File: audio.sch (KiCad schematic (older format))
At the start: 47 parts, among them Q11 BC546, Q12 BC546, Q13 BC546, Q14 BC546, U4 TL072

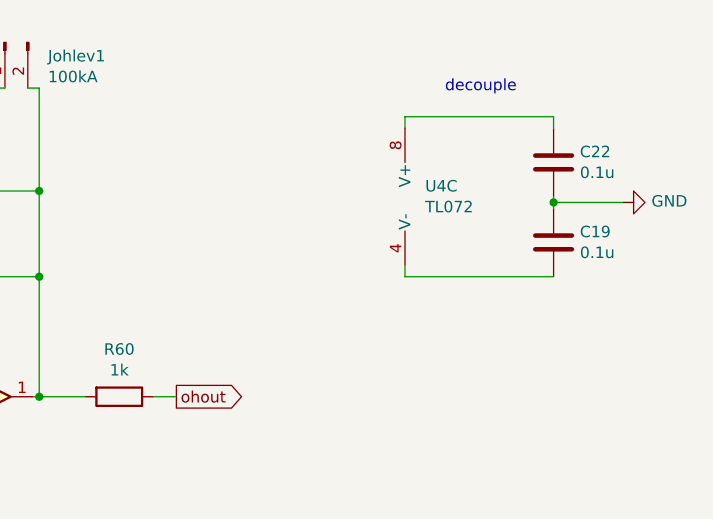
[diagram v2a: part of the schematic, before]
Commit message: fixup noise generator connections
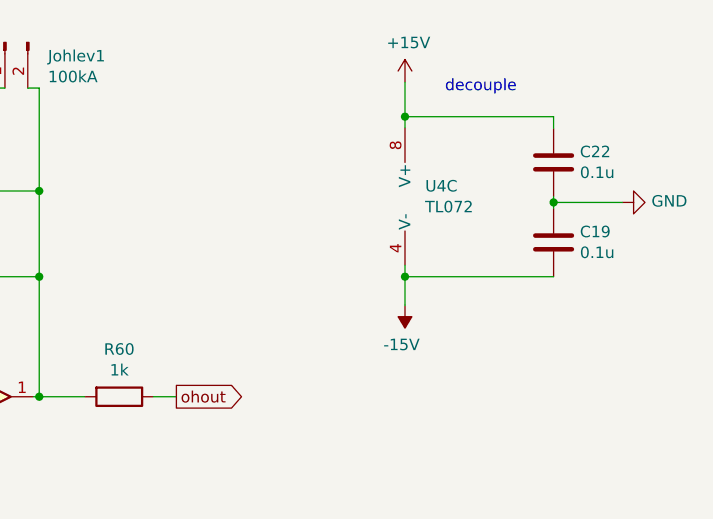
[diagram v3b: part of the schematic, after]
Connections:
- net +15V: now also C22.1, U4.8 (V+)
- net -15V: now also C19.2, U4.4 (V-)
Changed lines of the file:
@@
 EESchema Schematic File Version 4
 LIBS:808-hats-cache
-LIBS:shift-triggers-cache
-LIBS:mod-dac-cache
 EELAYER 26 0
 EELAYER END
@@
 Text Notes 9025 1000 0    50   ~ 0
 decouple
+$Comp
+L power:+15V #PWR?
+U 1 1 5CB7A0F9
+P 8850 950
+AR Path="/5CB7A0F9" Ref="#PWR?"  Part="1"
+AR Path="/5CC0DBBF/5CB7A0F9" Ref="#PWR0148"  Part="1"
+F 0 "#PWR0148" H 8850 800 50  0001 C CNN
+F 1 "+15V" H 8865 1123 50  0000 C CNN
+F 2 "" H 8850 950 50  0001 C CNN
+F 3 "" H 8850 950 50  0001 C CNN
+	1    8850 950
+	1    0    0    -1
+$EndComp
+$Comp
+L power:-15V #PWR?
+U 1 1 5CB7A166
+P 8850 1925
+AR Path="/5CB7A166" Ref="#PWR?"  Part="1"
+AR Path="/5CC0DBBF/5CB7A166" Ref="#PWR0149"  Part="1"
+F 0 "#PWR0149" H 8850 2025 50  0001 C CNN
+F 1 "-15V" H 8865 2098 50  0000 C CNN
+F 2 "" H 8850 1925 50  0001 C CNN
+F 3 "" H 8850 1925 50  0001 C CNN
+	1    8850 1925
+	-1   0    0    1
+$EndComp
+Wire Wire Line
+	8850 1800 8850 1925
+Connection ~ 8850 1800
+Wire Wire Line
+	8850 1100 8850 950
+Connection ~ 8850 1100
 $EndSCHEMATC

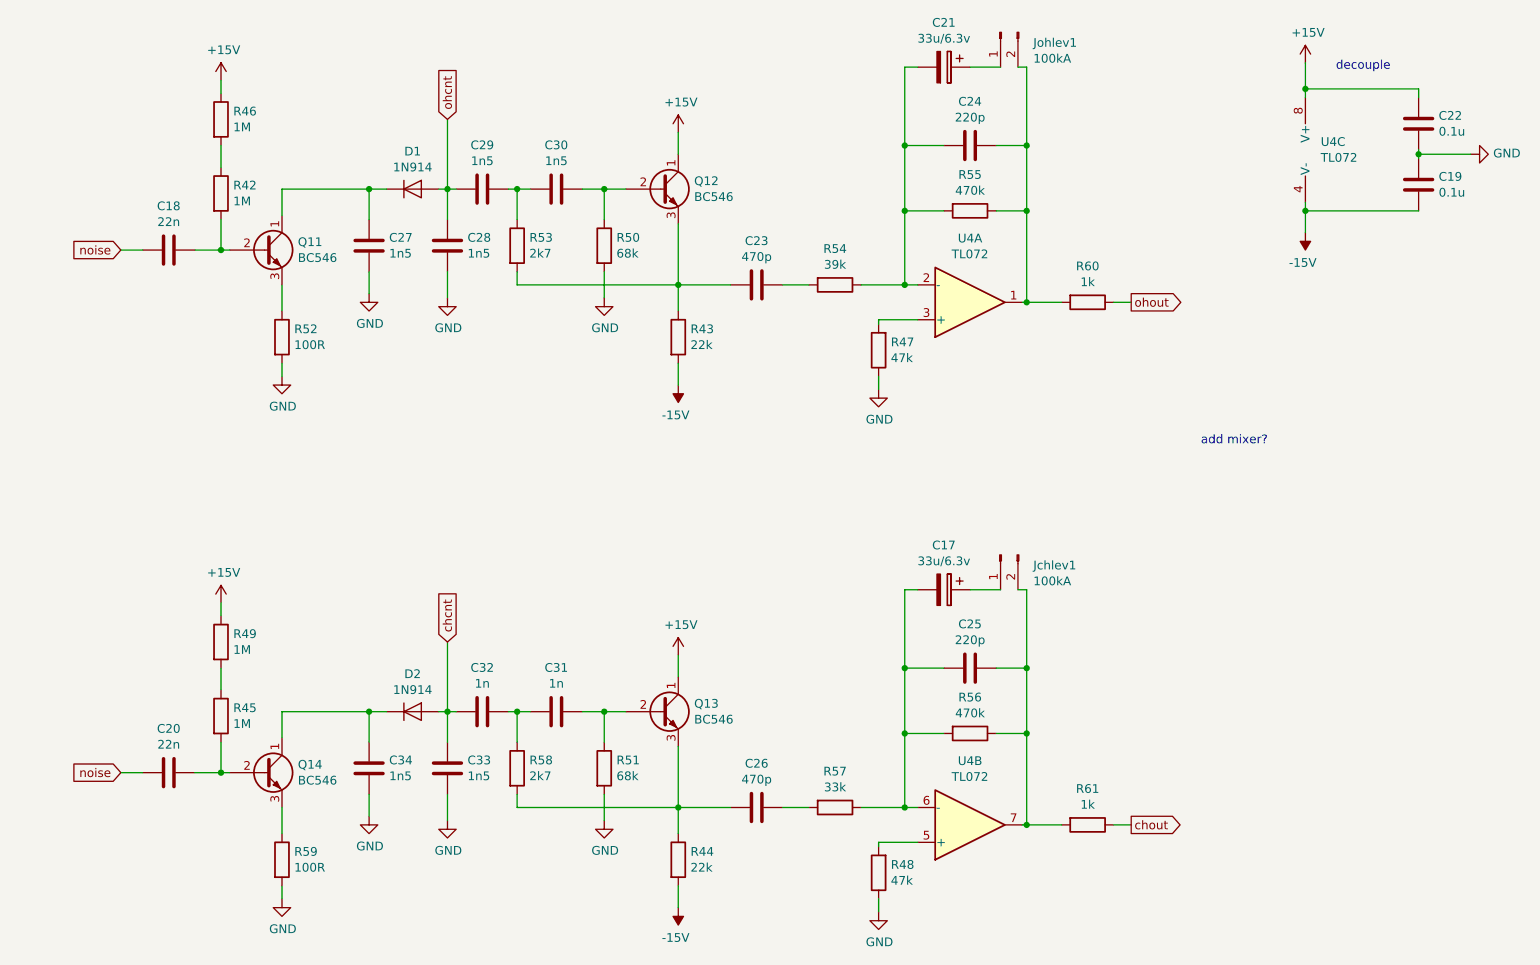
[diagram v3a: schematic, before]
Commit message: added filter mod
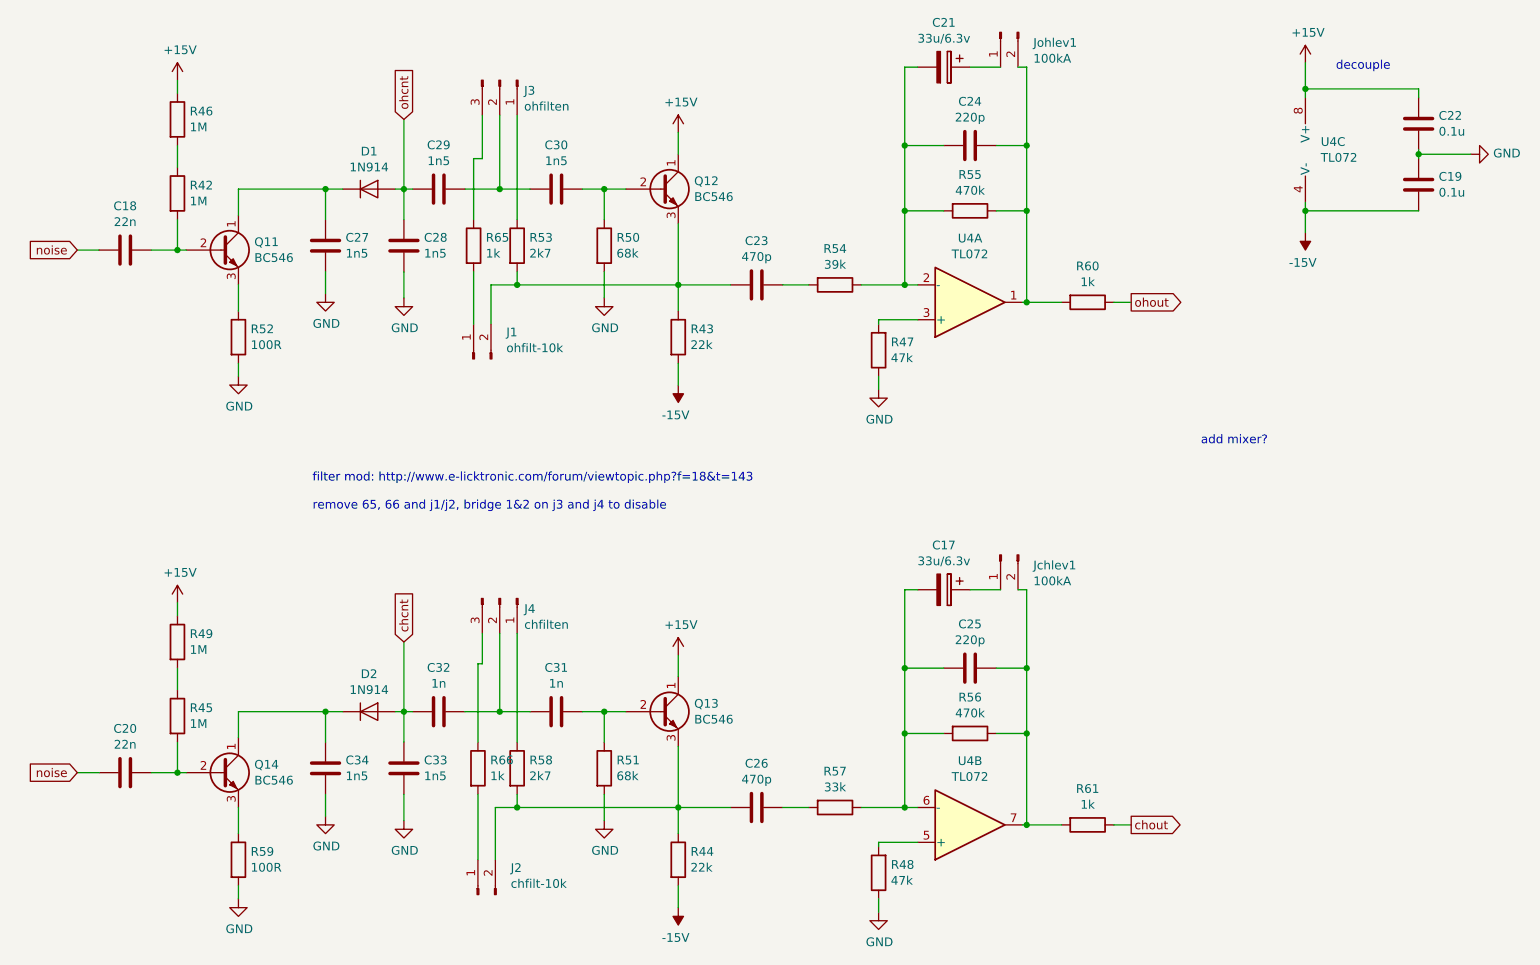
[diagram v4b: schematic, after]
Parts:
- added J1: ohfilt-10k, symbol Connector:Conn_01x02_Male
- added J2: chfilt-10k, symbol Connector:Conn_01x02_Male
- added J3: ohfilten, symbol Connector:Conn_01x03_Male
- added J4: chfilten, symbol Connector:Conn_01x03_Male
- added R65, R66: 1k, symbol Device:R
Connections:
- net at C29.2, C30.1: now also J3.2 (Pin_2); no longer R53.1
- net at C23.1, Q12.3 (E), R43.1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: now also J1.2 (Pin_2)
- net at C31.1, C32.2: now also J4.2 (Pin_2); no longer R58.1
- net at C26.1, Q13.3 (E), R44.1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: now also J2.2 (Pin_2)
- new net: J3.1 (Pin_1), R53.1
- new net: J3.3 (Pin_3), R65.1
- new net: J1.1 (Pin_1), R65.2
- new net: J4.1 (Pin_1), R58.1
- new net: J4.3 (Pin_3), R66.1
- new net: J2.1 (Pin_1), R66.2
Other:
- note added: "filter mod: http://www.e-licktronic.com/forum/viewtopic.php?f=18&t=143\n\nremove 65, 66 and j1/j2, bridge 1&2 on j3 and j4 to disable"
- moved on the sheet: C18, C20, C27, C28, C29, C32, C33, C34, D1, D2, Q11, Q14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

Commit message: selected some parts
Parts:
- C17: footprint (none) -> Capacitor_THT:CP_Radial_D7.5mm_P2.50mm
- J1, J2, Jchlev1, Johlev1: footprint (none) -> Connector_PinHeader_2.54mm:PinHeader_1x02_P2.54mm_Vertical
- J3, J4: footprint (none) -> Connector_PinHeader_2.54mm:PinHeader_1x03_P2.54mm_Vertical
- Q11, Q12, Q13, Q14: footprint Package_TO_SOT_THT:TO-92_Inline -> Package_TO_SOT_THT:TO-92L_Inline
- R42, R43, R44, R45, R46, R47, R48, R49, R50, R51, R52, R53, R54, R55, R56, R57, R58, R59, R60, R61, R65, R66: footprint (none) -> Resistor_THT:R_Axial_DIN0204_L3.6mm_D1.6mm_P7.62mm_Horizontal
- U4: footprint (none) -> Package_DIP:DIP-8_W7.62mm_LongPads
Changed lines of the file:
@@
 F 0 "R42" H 2445 1746 50  0000 L CNN
 F 1 "1M" H 2445 1655 50  0000 L CNN
-F 2 "" V 2305 1700 50  0001 C CNN
+F 2 "Resistor_THT:R_Axial_DIN0204_L3.6mm_D1.6mm_P7.62mm_Horizontal" V 2305 1700 50  0001 C CNN
 F 3 "~" H 2375 1700 50  0001 C CNN
 	1    2375 1700
@@
 F 0 "R46" H 2445 1321 50  0000 L CNN
 F 1 "1M" H 2445 1230 50  0000 L CNN
-F 2 "" V 2305 1275 50  0001 C CNN
+F 2 "Resistor_THT:R_Axial_DIN0204_L3.6mm_D1.6mm_P7.62mm_Horizontal" V 2305 1275 50  0001 C CNN
 F 3 "~" H 2375 1275 50  0001 C CNN
 	1    2375 1275
@@
 F 0 "Q11" H 2816 2071 50  0000 L CNN
 F 1 "BC546" H 2816 1980 50  0000 L CNN
-F 2 "Package_TO_SOT_THT:TO-92_Inline" H 2825 1950 50  0001 L CIN
+F 2 "Package_TO_SOT_THT:TO-92L_Inline" H 2825 1950 50  0001 L CIN
 F 3 "http://www.fairchildsemi.com/ds/BC/BC547.pdf" H 2625 2025 50  0001 L CNN
 	1    2625 2025
@@
 F 0 "R52" H 2795 2571 50  0000 L CNN
 F 1 "100R" H 2795 2480 50  0000 L CNN
-F 2 "" V 2655 2525 50  0001 C CNN
+F 2 "Resistor_THT:R_Axial_DIN0204_L3.6mm_D1.6mm_P7.62mm_Horizontal" V 2655 2525 50  0001 C CNN
 F 3 "~" H 2725 2525 50  0001 C CNN
 	1    2725 2525
@@
 F 0 "R53" H 4395 2046 50  0000 L CNN
 F 1 "2k7" H 4395 1955 50  0000 L CNN
-F 2 "" V 4255 2000 50  0001 C CNN
+F 2 "Resistor_THT:R_Axial_DIN0204_L3.6mm_D1.6mm_P7.62mm_Horizontal" V 4255 2000 50  0001 C CNN
 F 3 "~" H 4325 2000 50  0001 C CNN
 	1    4325 2000
@@
 F 0 "R50" H 4895 2046 50  0000 L CNN
 F 1 "68k" H 4895 1955 50  0000 L CNN
-F 2 "" V 4755 2000 50  0001 C CNN
+F 2 "Resistor_THT:R_Axial_DIN0204_L3.6mm_D1.6mm_P7.62mm_Horizontal" V 4755 2000 50  0001 C CNN
 F 3 "~" H 4825 2000 50  0001 C CNN
 	1    4825 2000
@@
 F 0 "Q12" H 5341 1721 50  0000 L CNN
 F 1 "BC546" H 5341 1630 50  0000 L CNN
-F 2 "Package_TO_SOT_THT:TO-92_Inline" H 5350 1600 50  0001 L CIN
+F 2 "Package_TO_SOT_THT:TO-92L_Inline" H 5350 1600 50  0001 L CIN
 F 3 "http://www.fairchildsemi.com/ds/BC/BC547.pdf" H 5150 1675 50  0001 L CNN
 	1    5150 1675
@@
 F 0 "R43" H 5320 2571 50  0000 L CNN
 F 1 "22k" H 5320 2480 50  0000 L CNN
-F 2 "" V 5180 2525 50  0001 C CNN
+F 2 "Resistor_THT:R_Axial_DIN0204_L3.6mm_D1.6mm_P7.62mm_Horizontal" V 5180 2525 50  0001 C CNN
 F 3 "~" H 5250 2525 50  0001 C CNN
 	1    5250 2525
@@
 F 0 "R54" V 5943 2225 50  0000 C CNN
 F 1 "39k" V 6034 2225 50  0000 C CNN
-F 2 "" V 6080 2225 50  0001 C CNN
+F 2 "Resistor_THT:R_Axial_DIN0204_L3.6mm_D1.6mm_P7.62mm_Horizontal" V 6080 2225 50  0001 C CNN
 F 3 "~" H 6150 2225 50  0001 C CNN
 	1    6150 2225
@@
 F 0 "U4" H 6925 1958 50  0000 C CNN
 F 1 "TL072" H 6925 2049 50  0000 C CNN
-F 2 "" H 6925 2325 50  0001 C CNN
+F 2 "Package_DIP:DIP-8_W7.62mm_LongPads" H 6925 2325 50  0001 C CNN
 F 3 "http://www.ti.com/lit/ds/symlink/tl071.pdf" H 6925 2325 50  0001 C CNN
 	1    6925 2325
@@
 F 0 "R47" H 6330 2554 50  0000 R CNN
 F 1 "47k" H 6330 2645 50  0000 R CNN
-F 2 "" V 6330 2600 50  0001 C CNN
+F 2 "Resistor_THT:R_Axial_DIN0204_L3.6mm_D1.6mm_P7.62mm_Horizontal" V 6330 2600 50  0001 C CNN
 F 3 "~" H 6400 2600 50  0001 C CNN
 	1    6400 2600
@@
 F 0 "R55" V 6718 1800 50  0000 C CNN
 F 1 "470k" V 6809 1800 50  0000 C CNN
-F 2 "" V 6855 1800 50  0001 C CNN
+F 2 "Resistor_THT:R_Axial_DIN0204_L3.6mm_D1.6mm_P7.62mm_Horizontal" V 6855 1800 50  0001 C CNN
 F 3 "~" H 6925 1800 50  0001 C CNN
 	1    6925 1800
@@
 F 0 "Johlev1" V 7160 587 50  0000 R CNN
 F 1 "100kA" V 7251 587 50  0000 R CNN
-F 2 "" H 7100 775 50  0001 C CNN
+F 2 "Connector_PinHeader_2.54mm:PinHeader_1x02_P2.54mm_Vertical" H 7100 775 50  0001 C CNN
 F 3 "~" H 7100 775 50  0001 C CNN
 	1    7100 775
@@
 F 0 "R60" V 7393 2325 50  0000 C CNN
 F 1 "1k" V 7484 2325 50  0000 C CNN
-F 2 "" V 7530 2325 50  0001 C CNN
+F 2 "Resistor_THT:R_Axial_DIN0204_L3.6mm_D1.6mm_P7.62mm_Horizontal" V 7530 2325 50  0001 C CNN
 F 3 "~" H 7600 2325 50  0001 C CNN
 	1    7600 2325
@@
 F 0 "R45" H 2445 4746 50  0000 L CNN
 F 1 "1M" H 2445 4655 50  0000 L CNN
-F 2 "" V 2305 4700 50  0001 C CNN
+F 2 "Resistor_THT:R_Axial_DIN0204_L3.6mm_D1.6mm_P7.62mm_Horizontal" V 2305 4700 50  0001 C CNN
 F 3 "~" H 2375 4700 50  0001 C CNN
 	1    2375 4700
@@
 F 0 "R49" H 2445 4321 50  0000 L CNN
 F 1 "1M" H 2445 4230 50  0000 L CNN
-F 2 "" V 2305 4275 50  0001 C CNN
+F 2 "Resistor_THT:R_Axial_DIN0204_L3.6mm_D1.6mm_P7.62mm_Horizontal" V 2305 4275 50  0001 C CNN
 F 3 "~" H 2375 4275 50  0001 C CNN
 	1    2375 4275
@@
 F 0 "Q14" H 2816 5071 50  0000 L CNN
 F 1 "BC546" H 2816 4980 50  0000 L CNN
-F 2 "Package_TO_SOT_THT:TO-92_Inline" H 2825 4950 50  0001 L CIN
+F 2 "Package_TO_SOT_THT:TO-92L_Inline" H 2825 4950 50  0001 L CIN
 F 3 "http://www.fairchildsemi.com/ds/BC/BC547.pdf" H 2625 5025 50  0001 L CNN
 	1    2625 5025
@@
 F 0 "R59" H 2795 5571 50  0000 L CNN
 F 1 "100R" H 2795 5480 50  0000 L CNN
-F 2 "" V 2655 5525 50  0001 C CNN
+F 2 "Resistor_THT:R_Axial_DIN0204_L3.6mm_D1.6mm_P7.62mm_Horizontal" V 2655 5525 50  0001 C CNN
 F 3 "~" H 2725 5525 50  0001 C CNN
 	1    2725 5525
@@
 F 0 "R58" H 4395 5046 50  0000 L CNN
 F 1 "2k7" H 4395 4955 50  0000 L CNN
-F 2 "" V 4255 5000 50  0001 C CNN
+F 2 "Resistor_THT:R_Axial_DIN0204_L3.6mm_D1.6mm_P7.62mm_Horizontal" V 4255 5000 50  0001 C CNN
 F 3 "~" H 4325 5000 50  0001 C CNN
 	1    4325 5000
@@
 F 0 "R51" H 4895 5046 50  0000 L CNN
 F 1 "68k" H 4895 4955 50  0000 L CNN
-F 2 "" V 4755 5000 50  0001 C CNN
+F 2 "Resistor_THT:R_Axial_DIN0204_L3.6mm_D1.6mm_P7.62mm_Horizontal" V 4755 5000 50  0001 C CNN
 F 3 "~" H 4825 5000 50  0001 C CNN
 	1    4825 5000
@@
 F 0 "Q13" H 5341 4721 50  0000 L CNN
 F 1 "BC546" H 5341 4630 50  0000 L CNN
-F 2 "Package_TO_SOT_THT:TO-92_Inline" H 5350 4600 50  0001 L CIN
+F 2 "Package_TO_SOT_THT:TO-92L_Inline" H 5350 4600 50  0001 L CIN
 F 3 "http://www.fairchildsemi.com/ds/BC/BC547.pdf" H 5150 4675 50  0001 L CNN
 	1    5150 4675
@@
 F 0 "R44" H 5320 5571 50  0000 L CNN
 F 1 "22k" H 5320 5480 50  0000 L CNN
-F 2 "" V 5180 5525 50  0001 C CNN
+F 2 "Resistor_THT:R_Axial_DIN0204_L3.6mm_D1.6mm_P7.62mm_Horizontal" V 5180 5525 50  0001 C CNN
 F 3 "~" H 5250 5525 50  0001 C CNN
 	1    5250 5525
@@
 F 0 "R57" V 5943 5225 50  0000 C CNN
 F 1 "33k" V 6034 5225 50  0000 C CNN
-F 2 "" V 6080 5225 50  0001 C CNN
+F 2 "Resistor_THT:R_Axial_DIN0204_L3.6mm_D1.6mm_P7.62mm_Horizontal" V 6080 5225 50  0001 C CNN
 F 3 "~" H 6150 5225 50  0001 C CNN
 	1    6150 5225
@@
 F 0 "U4" H 6925 4958 50  0000 C CNN
 F 1 "TL072" H 6925 5049 50  0000 C CNN
-F 2 "" H 6925 5325 50  0001 C CNN
+F 2 "Package_DIP:DIP-8_W7.62mm_LongPads" H 6925 5325 50  0001 C CNN
 F 3 "http://www.ti.com/lit/ds/symlink/tl071.pdf" H 6925 5325 50  0001 C CNN
 	2    6925 5325
@@
 F 0 "R48" H 6330 5554 50  0000 R CNN
 F 1 "47k" H 6330 5645 50  0000 R CNN
-F 2 "" V 6330 5600 50  0001 C CNN
+F 2 "Resistor_THT:R_Axial_DIN0204_L3.6mm_D1.6mm_P7.62mm_Horizontal" V 6330 5600 50  0001 C CNN
 F 3 "~" H 6400 5600 50  0001 C CNN
 	1    6400 5600
@@
 F 0 "R56" V 6718 4800 50  0000 C CNN
 F 1 "470k" V 6809 4800 50  0000 C CNN
-F 2 "" V 6855 4800 50  0001 C CNN
+F 2 "Resistor_THT:R_Axial_DIN0204_L3.6mm_D1.6mm_P7.62mm_Horizontal" V 6855 4800 50  0001 C CNN
 F 3 "~" H 6925 4800 50  0001 C CNN
 	1    6925 4800
@@
 F 0 "C17" V 6520 3975 50  0000 C CNN
 F 1 "33u/6.3v" V 6611 3975 50  0000 C CNN
-F 2 "" H 6813 3825 50  0001 C CNN
+F 2 "Capacitor_THT:CP_Radial_D7.5mm_P2.50mm" H 6813 3825 50  0001 C CNN
 F 3 "~" H 6775 3975 50  0001 C CNN
 	1    6775 3975
@@
 F 0 "Jchlev1" V 7160 3587 50  0000 R CNN
 F 1 "100kA" V 7251 3587 50  0000 R CNN
-F 2 "" H 7100 3775 50  0001 C CNN
+F 2 "Connector_PinHeader_2.54mm:PinHeader_1x02_P2.54mm_Vertical" H 7100 3775 50  0001 C CNN
 F 3 "~" H 7100 3775 50  0001 C CNN
 	1    7100 3775
@@
 F 0 "R61" V 7393 5325 50  0000 C CNN
 F 1 "1k" V 7484 5325 50  0000 C CNN
-F 2 "" V 7530 5325 50  0001 C CNN
+F 2 "Resistor_THT:R_Axial_DIN0204_L3.6mm_D1.6mm_P7.62mm_Horizontal" V 7530 5325 50  0001 C CNN
 F 3 "~" H 7600 5325 50  0001 C CNN
 	1    7600 5325
@@
 F 0 "U4" H 8562 1496 50  0000 R CNN
 F 1 "TL072" H 8562 1405 50  0000 R CNN
-F 2 "" H 8750 1450 50  0001 C CNN
+F 2 "Package_DIP:DIP-8_W7.62mm_LongPads" H 8750 1450 50  0001 C CNN
 F 3 "http://www.ti.com/lit/ds/symlink/tl071.pdf" H 8750 1450 50  0001 C CNN
 	3    8750 1450
@@
 F 0 "J3" V 4285 1190 50  0000 L CNN
 F 1 "ohfilten" V 4376 1190 50  0000 L CNN
-F 2 "" H 4225 1050 50  0001 C CNN
+F 2 "Connector_PinHeader_2.54mm:PinHeader_1x03_P2.54mm_Vertical" H 4225 1050 50  0001 C CNN
 F 3 "~" H 4225 1050 50  0001 C CNN
 	1    4225 1050
@@
 F 0 "R65" H 4145 2046 50  0000 L CNN
 F 1 "1k" H 4145 1955 50  0000 L CNN
-F 2 "" V 4005 2000 50  0001 C CNN
+F 2 "Resistor_THT:R_Axial_DIN0204_L3.6mm_D1.6mm_P7.62mm_Horizontal" V 4005 2000 50  0001 C CNN
 F 3 "~" H 4075 2000 50  0001 C CNN
 	1    4075 2000
@@
 F 0 "J1" V 4228 2462 50  0000 R CNN
 F 1 "ohfilt-10k" V 4137 2462 50  0000 R CNN
-F 2 "" H 4075 2650 50  0001 C CNN
+F 2 "Connector_PinHeader_2.54mm:PinHeader_1x02_P2.54mm_Vertical" H 4075 2650 50  0001 C CNN
 F 3 "~" H 4075 2650 50  0001 C CNN
 	1    4075 2650
@@
 F 0 "J4" V 4285 4166 50  0000 L CNN
 F 1 "chfilten" V 4376 4166 50  0000 L CNN
-F 2 "" H 4225 4025 50  0001 C CNN
+F 2 "Connector_PinHeader_2.54mm:PinHeader_1x03_P2.54mm_Vertical" H 4225 4025 50  0001 C CNN
 F 3 "~" H 4225 4025 50  0001 C CNN
 	1    4225 4025
@@
 F 0 "R66" H 4170 5046 50  0000 L CNN
 F 1 "1k" H 4170 4955 50  0000 L CNN
-F 2 "" V 4030 5000 50  0001 C CNN
+F 2 "Resistor_THT:R_Axial_DIN0204_L3.6mm_D1.6mm_P7.62mm_Horizontal" V 4030 5000 50  0001 C CNN
 F 3 "~" H 4100 5000 50  0001 C CNN
 	1    4100 5000
@@
 F 0 "J2" V 4253 5537 50  0000 R CNN
 F 1 "chfilt-10k" V 4162 5537 50  0000 R CNN
-F 2 "" H 4100 5725 50  0001 C CNN
+F 2 "Connector_PinHeader_2.54mm:PinHeader_1x02_P2.54mm_Vertical" H 4100 5725 50  0001 C CNN
 F 3 "~" H 4100 5725 50  0001 C CNN
 	1    4100 5725
